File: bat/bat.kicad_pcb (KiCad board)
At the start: 2 copper layers, 94.4 x 48.5 mm, 21 parts, among them Q1 2N3904, Q2 2N3904, Q3 2N3904, SW1 SW_SPDT

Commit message: Another WIP
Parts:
- moved BT1 6.77 mm to (145.3, 100.2)
- moved C1 6.77 mm to (175.0, 93.4)
- moved C2 6.77 mm to (107.0, 105.3)
- moved C3 6.77 mm to (115.6, 93.4)
- moved D1 6.77 mm to (148.4, 85.3)
- moved D2 6.77 mm to (142.3, 85.3)
- moved Q1 6.77 mm to (115.6, 105.3)
- moved Q2 6.77 mm to (175.0, 100.2)
- moved Q3 6.77 mm to (182.6, 90.9)
- moved R1 6.77 mm to (129.8, 100.2)
- moved R2 6.77 mm to (160.8, 100.2)
- moved R3 6.77 mm to (160.8, 92.6)
- moved R4 6.77 mm to (129.8, 105.3)
- moved R5 6.77 mm to (120.0, 90.0)
- moved R6 6.77 mm to (160.8, 105.3)
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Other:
- board text added: "0"
- board text added: "1"

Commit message: Readmes
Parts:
- D1, D2: moved to B.Cu

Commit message: boom prask netopyr netopyr
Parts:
- Q3: value 2N3904 -> S8550
- R1, R2: value 10k -> 68k
- R3, R4: value 47k -> 100k
- R5: value 330 -> 47R
- R6: value 300k -> 47k
- moved Q3 5.10 mm to (182.6, 96.0), turned to 90 degrees
- moved BT1 0.10 mm to (145.3, 100.1)
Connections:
- Q3 pad 1: GND -> Net-(D1-K)
- Q3 pad 3: Net-(D1-K) -> GND
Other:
- board text added: "OFF"
- board text added: "ON"
- board text removed: "0"
- board text removed: "1"

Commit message: netopyr
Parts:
- removed the REF** at (112.5, 80.4)
- removed the REF** at (178.1, 80.4)
- removed the REF** at (101.6, 110.9)
- removed the REF** at (189.0, 110.9)
- added REF**: MountingHole_2.2mm_M2_DIN965_Pad, MountingHole:MountingHole_2.2mm_M2_DIN965_Pad, F.Cu at (172.3, 81.9)
- added REF**: MountingHole_2.2mm_M2_DIN965_Pad, MountingHole:MountingHole_2.2mm_M2_DIN965_Pad, F.Cu at (118.3, 81.9)
- D1, D2: moved to F.Cu
- moved Q2 13.7 mm to (181.0, 87.9), turned to 120 degrees
- moved SW1 10.8 mm to (173.1, 100.2), turned to 120 degrees
- moved C2 10.7 mm to (109.3, 94.9), turned to 150 degrees
- moved D1 7.85 mm to (140.5, 84.7)
- moved Q1 6.37 mm to (118.7, 99.8), turned to 150 degrees
- moved D2 5.30 mm to (147.5, 84.7), turned to 0 degrees
- moved C3 3.39 mm to (116.5, 90.2), turned to 150 degrees
- moved C1 2.86 mm to (174.1, 90.7), turned to -60 degrees
- moved R4 2.62 mm to (130.3, 107.9), turned to 150 degrees
- moved R6 2.62 mm to (160.3, 107.9), turned to 30 degrees
- moved Q3 2.56 mm to (185.0, 94.9), turned to 120 degrees
- moved R5 1.91 mm to (121.5, 88.8), turned to -30 degrees
- moved R3 1.37 mm to (160.3, 93.9), turned to 30 degrees
- moved R1 0.82 mm to (130.3, 100.9), turned to 150 degrees
- moved R2 0.82 mm to (160.3, 100.9), turned to 30 degrees
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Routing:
- net Net-(Q3-B): track 81.7 -> 0.00 mm
- net Net-(Q2-C): track 75.8 -> 0.00 mm
- net Net-(Q1-C): track 62.3 -> 0.00 mm
- net Net-(D1-K): track 48.4 -> 0.00 mm
- net Net-(BT1-+): track 41.3 -> 0.00 mm
- net Net-(D1-A): track 27.4 -> 0.00 mm
- net Net-(Q2-B): track 16.7 -> 0.00 mm
- net Net-(Q1-B): track 13.8 -> 0.00 mm
- removed copper zone on B.Cu, net +3V0
- removed copper zone on F.Cu, net GND
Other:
- board size 94.4 x 48.5 mm -> 87.2 x 48.5 mm

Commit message: Added cat-pin, bat, traffic light?
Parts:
- moved R3 13.5 mm to (160.3, 107.4)
- moved R6 13.5 mm to (160.3, 94.4)
- moved Q3 12.9 mm to (172.1, 94.2), turned to 30 degrees
- moved C1 6.95 mm to (177.6, 84.7)
- moved Q2 3.36 mm to (181.5, 91.2), turned to -60 degrees
- moved D1 2.55 mm to (143.1, 84.7), turned to 180 degrees
- moved C2 2.38 mm to (107.1, 93.9), turned to -30 degrees
- moved Q1 0.68 mm to (118.5, 100.4)
- moved R4 0.50 mm to (130.3, 107.4)
- moved R5 0.50 mm to (121.5, 89.3)
- moved REF** 0.50 mm to (145.3, 117.4)
- moved BT1 0.25 mm to (145.3, 100.2)
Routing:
- net Net-(Q2-C): track 0.00 -> 80.5 mm
- net Net-(Q1-C): track 0.00 -> 70.5 mm
- net Net-(Q3-B): track 0.00 -> 64.0 mm
- net Net-(BT1-+): track 0.00 -> 37.6 mm
- net Net-(D1-K): track 0.00 -> 35.8 mm
- net Net-(D1-A): track 0.00 -> 32.2 mm
- net Net-(Q2-B): track 0.00 -> 30.0 mm
- net Net-(Q1-B): track 0.00 -> 20.4 mm
- added copper zone on F.Cu, net +3V0
- added copper zone on B.Cu, net GND
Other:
- board size 87.2 x 48.5 mm -> 87.2 x 49.4 mm
- board text added: "0"
- board text added: "100k"
- board text added: "47R"
- board text added: "68k"
- board text added: "I"
- board text added: "S8550"
- board text added: "V2.0"
- board text added: "pajecistavebnice.cz"
- board text removed: "10k"
- board text removed: "300k"
- board text removed: "330"
- board text removed: "OFF"
- board text removed: "ON"
- board text removed: "V1.0"
- board text removed: "github.com/polaracep"

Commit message: Production version
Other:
- board text added: "OFF"
- board text added: "ON"
- board text removed: "0"
- board text removed: "I"

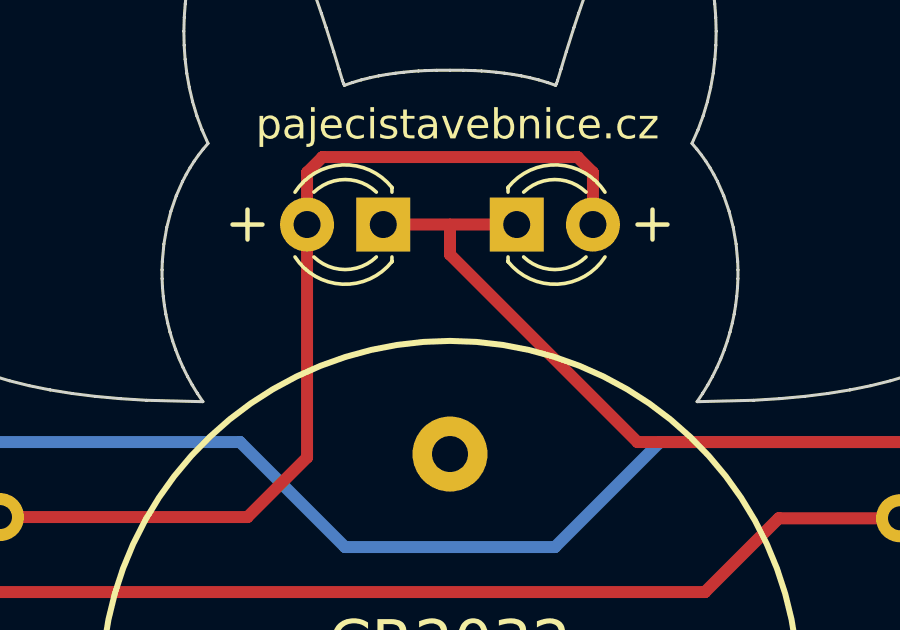
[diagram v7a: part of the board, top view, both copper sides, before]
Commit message: Bat modification
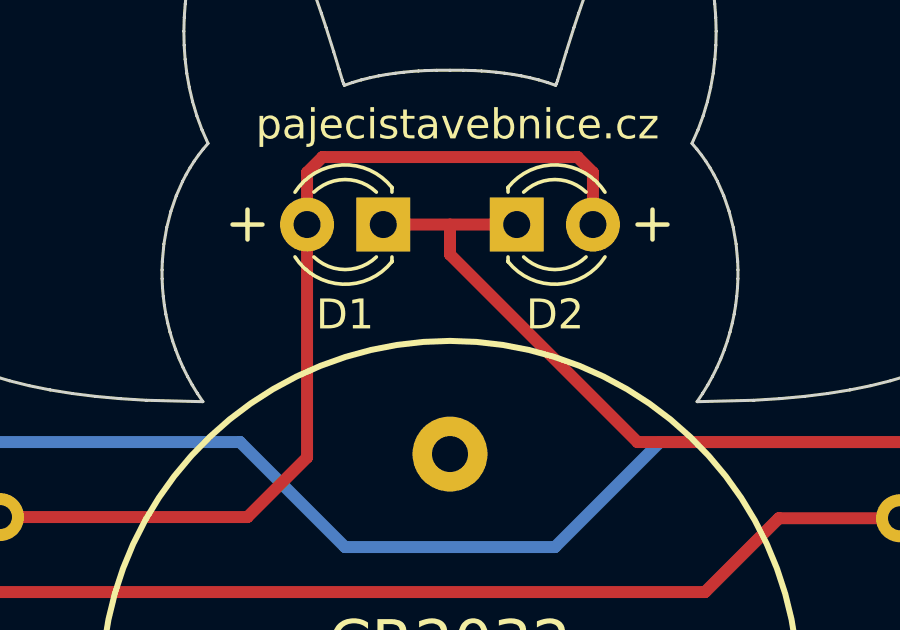
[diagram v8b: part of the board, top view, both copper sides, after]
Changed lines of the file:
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@@
 		(tags "LED diameter 3.0mm 2 pins")
 		(property "Reference" "D1"
-			(at 1.375 -2.950002 0)
+			(at 1.274999 -3.000001 0)
 			(layer "F.SilkS")
-			(hide yes)
 			(effects
 				(font
@@
 		(fp_arc
 			(start 0.6 1.7)
-			(mid 0.389183 1.423933)
+			(mid 0.389182 1.423934)
 			(end 0.217369 1.122045)
 			(stroke
@@
 		(tags "LED diameter 3.0mm 2 pins")
 		(property "Reference" "D2"
-			(at -2.027 0 -90)
+			(at 1.275 2.999999 180)
 			(layer "F.SilkS")
-			(hide yes)
 			(effects
 				(font
